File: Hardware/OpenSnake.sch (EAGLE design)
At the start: 36 parts, among them J1 microB, Q1 16MHZ, U1 ATMEGA328P_TQFP, U3 CH340G, U4 5V, Y2 12MHz

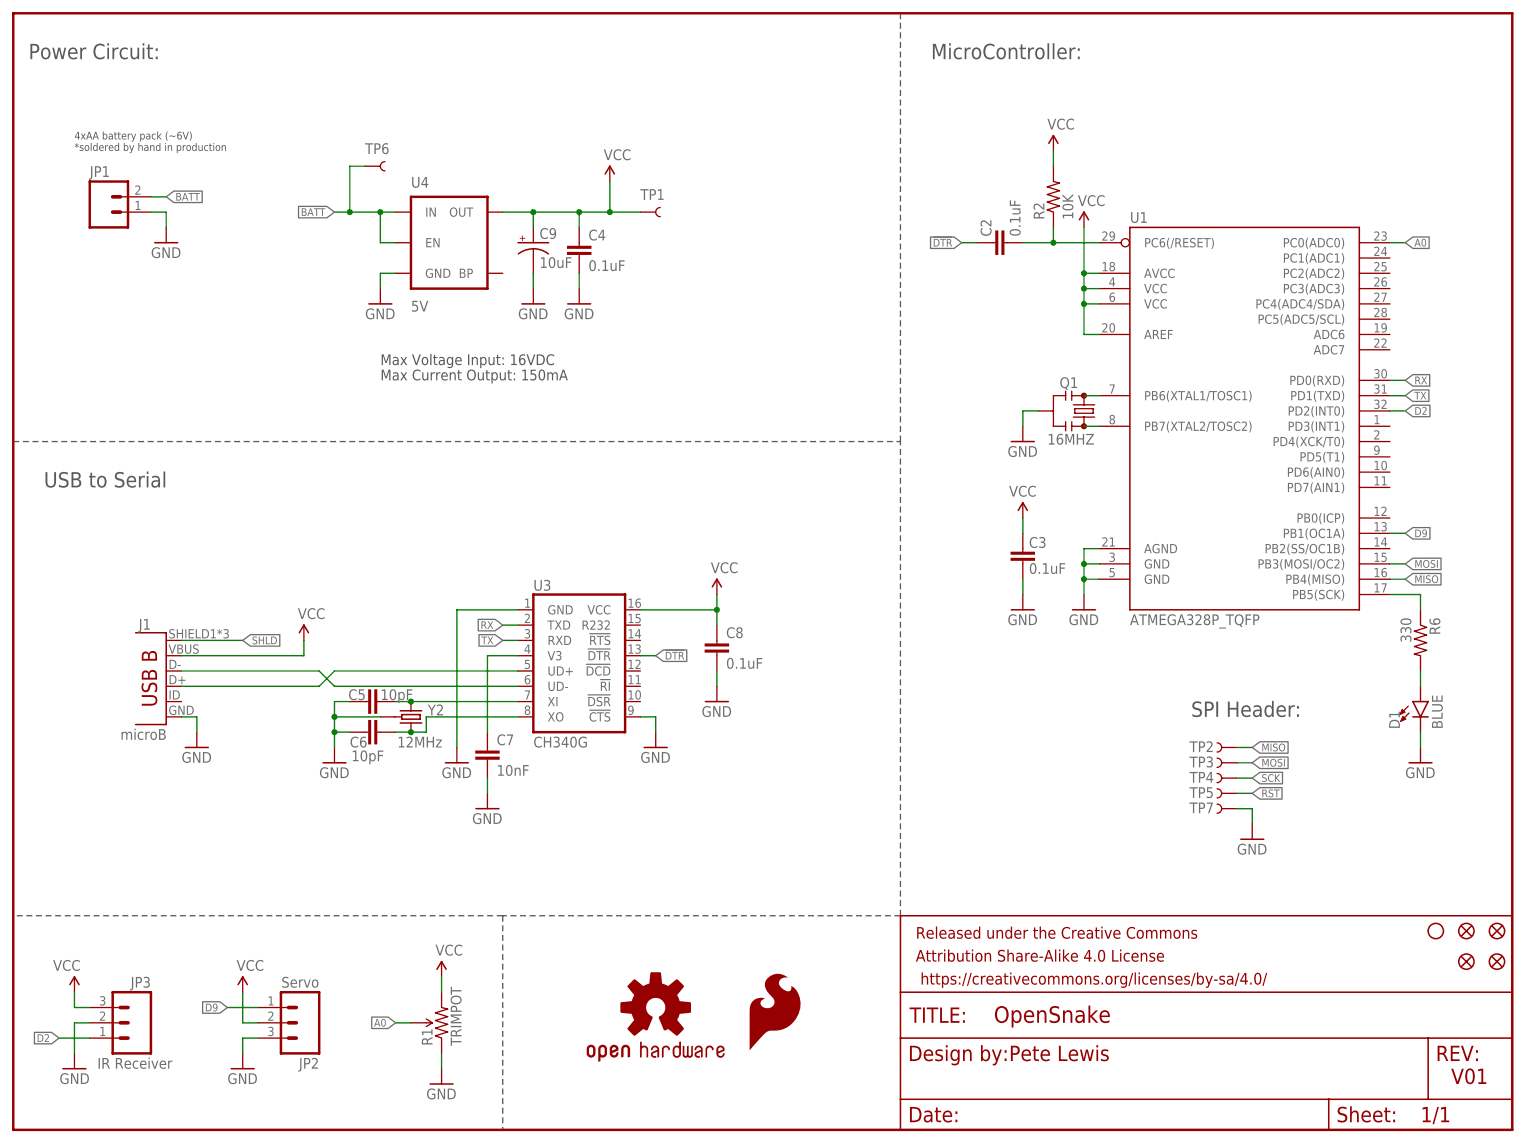
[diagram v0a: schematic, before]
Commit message: initial idea on pcb layout
the plan is to use some double sided tape and stick this to the side of the can. The 9V battery would also be stuck to the other side.
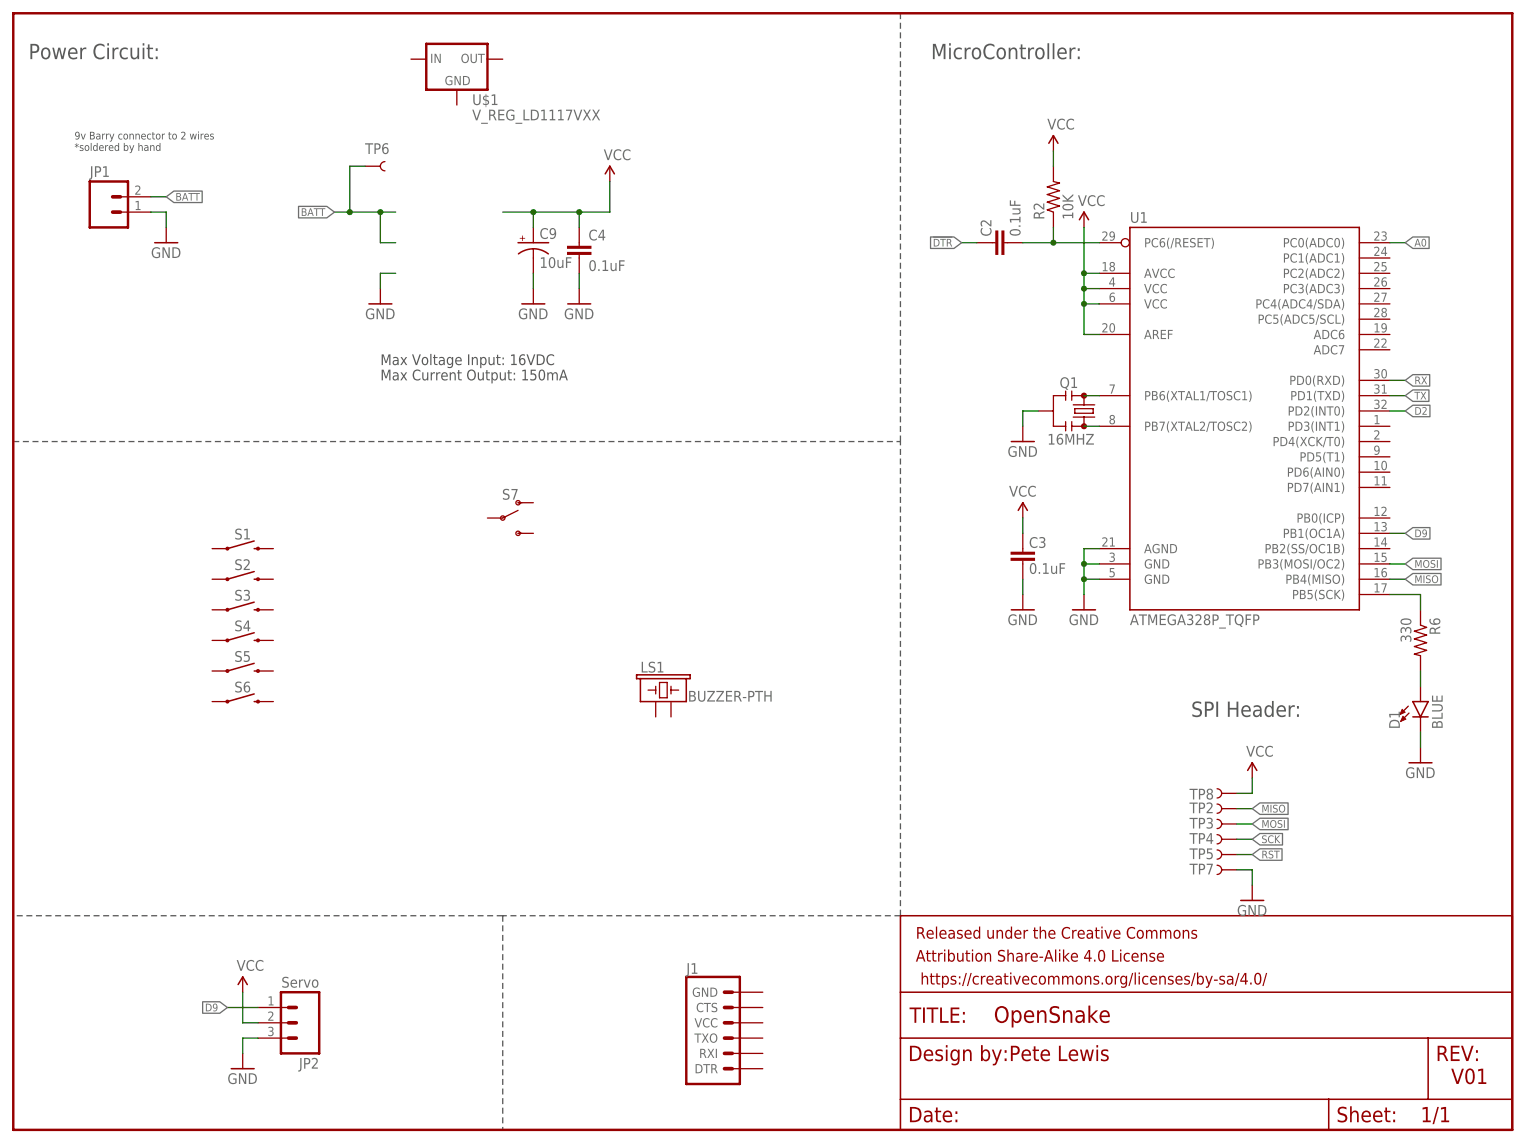
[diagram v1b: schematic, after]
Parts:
- removed C5, C6: 10pF, SparkFun-Capacitors:10PF-50V-5%(0603)
- removed C7: 10nF, SparkFun-Capacitors:10NF/10000PF-50V-10%(0603)
- removed C8: 0.1uF, SparkFun-Capacitors:0.1UF-25V(+80/-20%)(0603)
- removed FID1, FID2, FID3, FID4: FIDUCIALUFIDUCIAL, SparkFun-Aesthetics:FIDUCIALUFIDUCIAL
- removed H1: STAND-OFF, SparkFun-Hardware:STAND-OFF
- removed JP3: IR Receiver, Testing:M03LOCK
- removed LOGO1: SFE_LOGO_FLAME.1_INCH, SparkFun-Aesthetics:SFE_LOGO_FLAME.1_INCH
- removed LOGO2: OSHW-LOGOMINI, SparkFun-Aesthetics:OSHW-LOGOMINI
- removed R1: TRIMPOT, Jim-Resistors-to-Move:TRIMPOT-PTH-KNOB
- removed TP1: TEST-POINT3, SparkFun-Passives:TEST-POINT3
- removed U3: CH340G, SparkFun-DigitalIC:CH340GSMD
- removed U4: 5V, SparkFun-IC-Power:MIC52055V
- removed Y2: 12MHz, USB Basic:CRYSTAL-GROUNDED3.2X2.5
- added LS1: BUZZER-PTH, SparkFun-Electromechanical:BUZZER-PTH
- added S1, S2, S3, S4, S5, S6: MOMENTARY-SWITCH-SPST-PTH-6.0MM, SparkFun-Switches:MOMENTARY-SWITCH-SPST-PTH-6.0MM
- added S7: (no value), SparkFun-Switches:SWITCH-SPDT-PTH-11.6X4.0MM
- added TP8: TEST-POINT3, SparkFun-Passives:TEST-POINT3
- added U$1: V_REG_LD1117VXX, SparkFun-IC-Power:V_REG_LD1117VXX
- J1: value microB -> (none); device SparkFun-Connectors:USB-MICROB" -> SparkFun-Connectors:6_PIN_SERIAL_TARGETSILK
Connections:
- removed net N$3: C6.2, U3.XO, Y2.2
- removed net N$4: C5.2, U3.XI, Y2.1
- removed net N$5: J1.D+, U3.UD+
- removed net N$6: J1.D-, U3.UD-
- removed net SHLD: J1.SHIELD
- removed net V3: C7.1, U3.V3
- net !DTR: no longer U3.!DTR
- net A0: no longer R1.WIPER
- net BATT: no longer U4.EN, U4.IN
- net D2: no longer JP3.1
- net GND: no longer C5.1, C6.1, C7.2, C8.2, J1.GND, JP3.2, R1.CCW, U3.!CTS, U3.GND, U4.GND, Y2.GND
- net RX: no longer U3.TXD
- net TX: no longer U3.RXD
- net VCC: now also TP8.1; no longer C8.1, J1.VBUS, JP3.3, R1.CW, TP1.1, U3.VCC, U4.OUT
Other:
- note added: "9v Barry connector to 2 wires *soldered by hand"
- note removed: "4xAA battery pack (~6V) *soldered by hand in production"
- note removed: "USB to Serial"
- moved on the sheet: TP2, TP3, TP4, TP5, TP7

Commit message: v01 hardware ordered - Added mario logo to bottom silk -  and code started
-mario logo on bottom silk
-v01 hardware prototypes ordered
-Started working on the code using a simon says kit.
-got yes, no sound functions working
-got default tracks working and playing
-still needs servo control implemented, but currently mapped out in snake() function
-still needs button control, record feature and factory reset feature
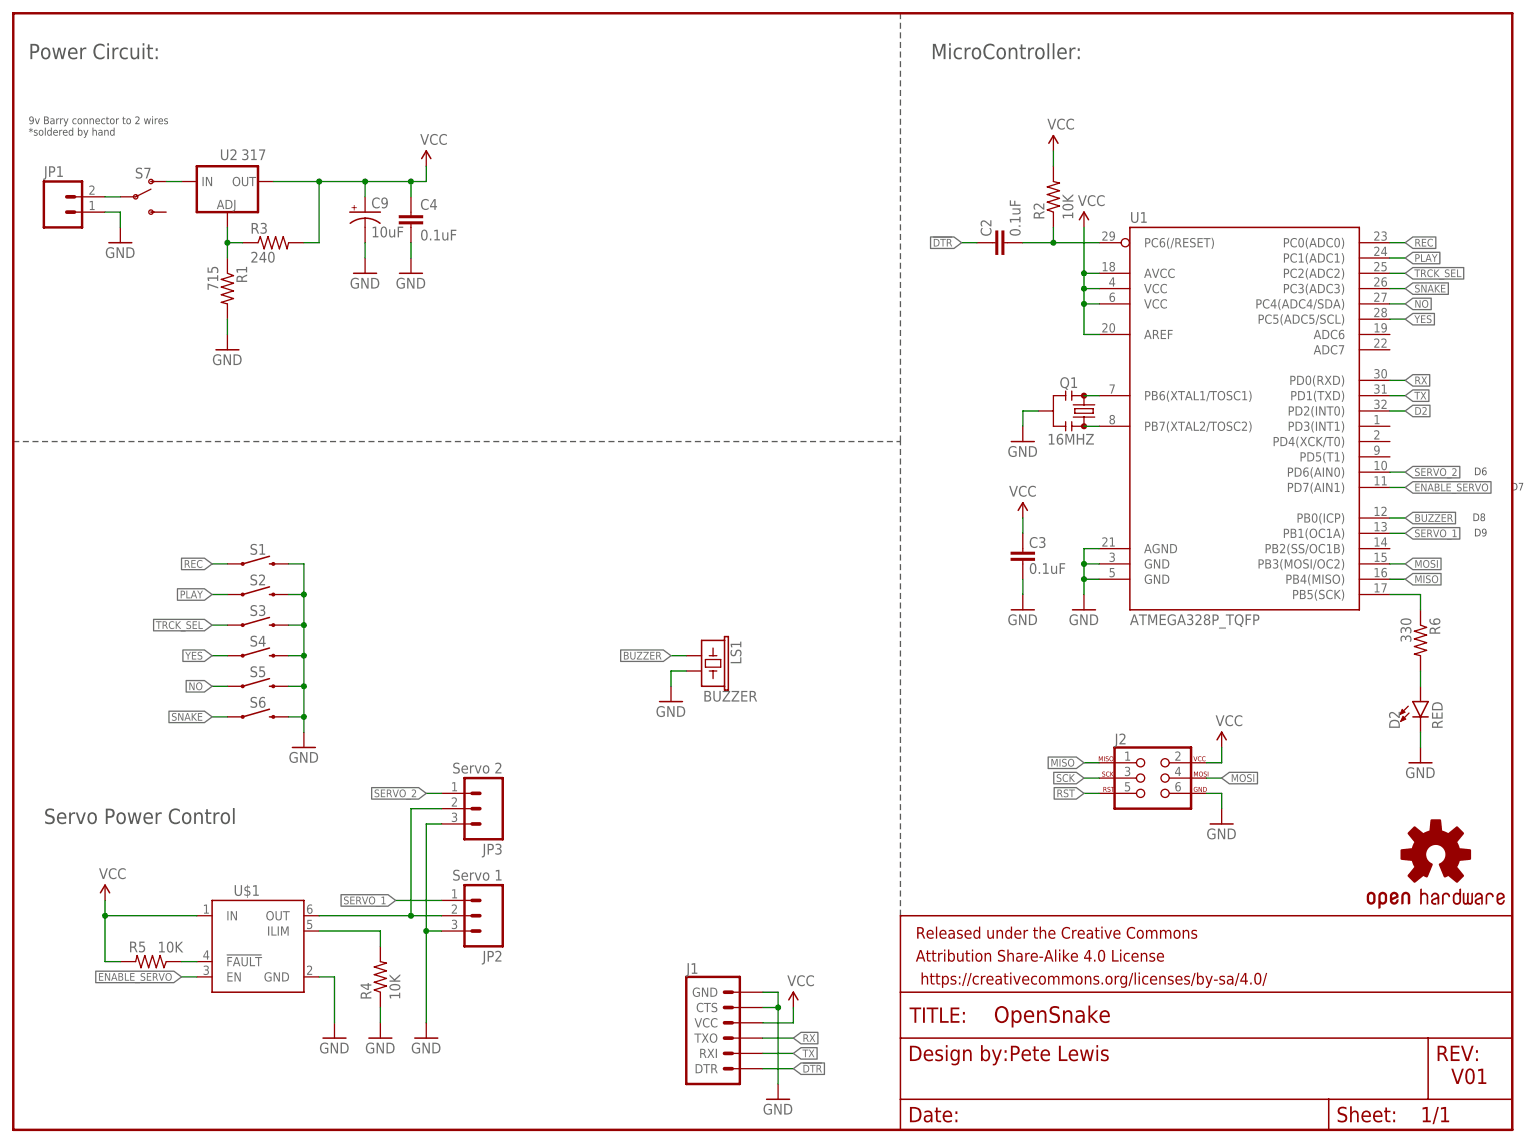
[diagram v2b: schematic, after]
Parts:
- removed D1: BLUE, SparkFun-LED:LED-BLUE1206
- removed TP2, TP3, TP4, TP5, TP6, TP7, TP8: TEST-POINT3, SparkFun-Passives:TEST-POINT3
- added D2: RED, SparkFun-LED:LED10MM
- added J2: AVR_SPI_PROG_3X2PTH, SparkFun-Connectors:AVR_SPI_PROG_3X2PTH
- added JP3: Servo 2, Testing:M03LOCK
- added LOGO1: OSHW-LOGOL, SparkFun-Aesthetics:OSHW-LOGOL
- added R1: 715, SparkFun-Resistors:330OHM1/10W1%(0603)
- added R3: 240, SparkFun-Resistors:330OHM1/10W1%(0603)
- added R4, R5: 10K, SparkFun-Resistors:10KOHM-1/10W-1%(0603)0603
- added U2: 317, SparkFun-IC-Power:V_REG_317SINK
- JP2: value Servo -> Servo 1
- LS1: value BUZZER-PTH -> BUZZER
- S1, S2, S3, S4, S5, S6: value MOMENTARY-SWITCH-SPST-PTH-6.0MM -> MOMENTARY-SWITCH-SPST-SMD-5.2MM-TALL; device SparkFun-Switches:MOMENTARY-SWITCH-SPST-PTH-6.0MM -> SparkFun-Switches:MOMENTARY-SWITCH-SPST-SMD-5.2MM-TALL
- U$1: value V_REG_LD1117VXX -> AP2553; device SparkFun-IC-Power:V_REG_LD1117VXX -> snake:AP2553
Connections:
- net D9 renamed SERVO_1
- removed net A0: U1.PC0(ADC0)
- removed net BATT: JP1.2, TP6.1
- new net BUZZER: LS1.1, U1.PB0(ICP)
- new net ENABLE_SERVO: U$1.EN, U1.PD7(AIN1)
- new net N$3: R1.1, R3.1, U2.ADJ
- new net N$4: JP1.2, S7.P
- new net N$5: S7.O, U2.IN
- new net N$6: JP2.2, JP3.2, U$1.OUT
- new net N$8: R4.2, U$1.ILIM
- new net N$9: R5.1, U$1.!FAULT
- new net NO: S5.1, U1.PC4(ADC4/SDA)
- new net PLAY: S2.1, U1.PC1(ADC1)
- new net REC: S1.1, U1.PC0(ADC0)
- new net SERVO_2: JP3.1, U1.PD6(AIN0)
- new net SNAKE: S6.1, U1.PC3(ADC3)
- new net TRCK_SEL: S3.1, U1.PC2(ADC2)
- new net YES: S4.1, U1.PC5(ADC5/SCL)
- net !DTR: now also J1.DTR
- net GND: now also D2.C, J1.CTS, J1.GND, J2.6, JP3.3, LS1.2, R1.2, R4.1, S1.2, S2.2, S3.2, S4.2, S5.2, S6.2, U$1.GND; no longer D1.C, TP7.1
- net MISO: now also J2.1; no longer TP2.1
- net MOSI: now also J2.4; no longer TP3.1
- net N$7: now also D2.A; no longer D1.A
- net RST: now also J2.5; no longer TP5.1
- net RX: now also J1.TXO
- net SCK: now also J2.3; no longer TP4.1
- net TX: now also J1.RXI
- net VCC: now also J1.VCC, J2.2, R3.2, R5.2, U$1.IN, U2.OUT; no longer JP2.2, TP8.1
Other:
- note added: "D6"
- note added: "D7"
- note added: "D8"
- note added: "D9"
- note added: "Servo Power Control"
- note removed: "Max Current Output: 150mA"
- note removed: "Max Voltage Input: 16VDC"
- note removed: "SPI Header:"
- moved on the sheet: C4, C9, JP1, JP2, LS1, S1, S2, S3, S4, S5, S6, S7

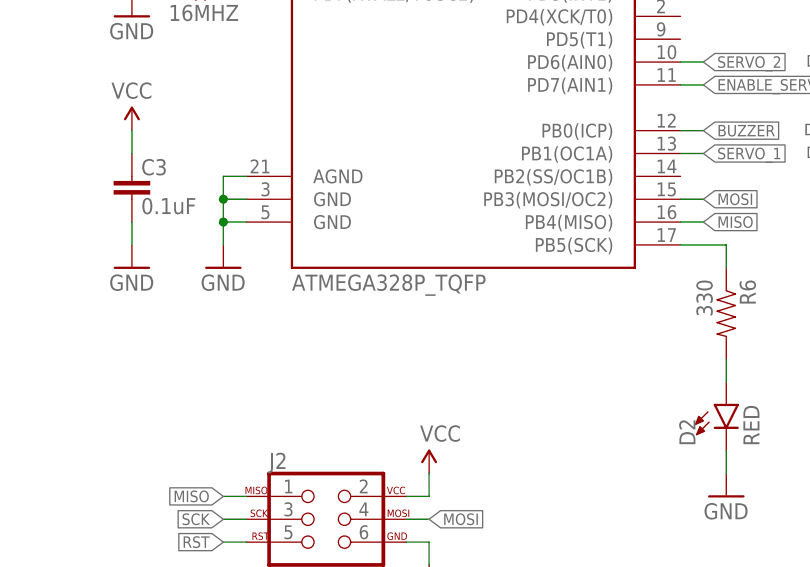
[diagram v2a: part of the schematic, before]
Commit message: Adjusted tValues for better assembly sheet, created assembly sheet PDF
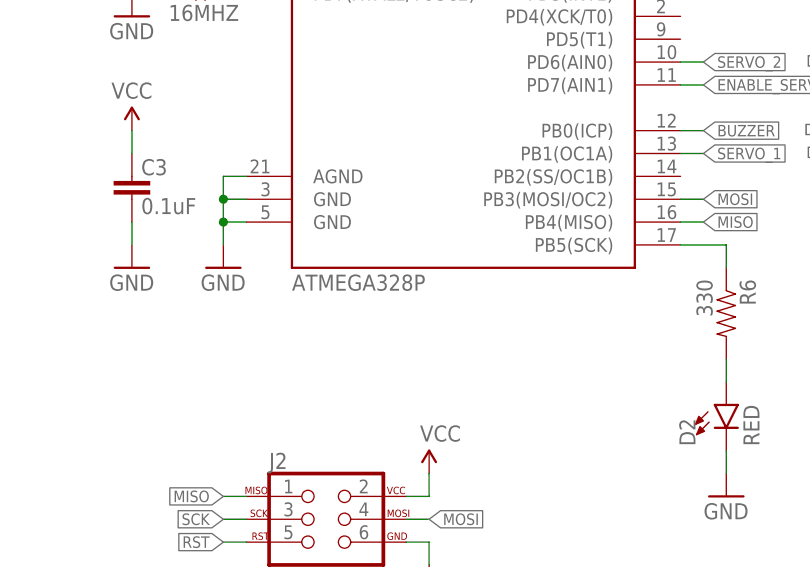
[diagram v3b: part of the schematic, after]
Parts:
- U1: value ATMEGA328P_TQFP -> ATMEGA328P
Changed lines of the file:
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@@
 <part name="GND5" library="SparkFun" deviceset="GND" device=""/>
 <part name="C2" library="SparkFun-Capacitors" deviceset="0.1UF-25V(+80/-20%)(0603)" device="" value="0.1uF"/>
-<part name="U1" library="SparkFun-DigitalIC" deviceset="ATMEGA328P_TQFP" device="" value="ATMEGA328P_TQFP"/>
+<part name="U1" library="SparkFun-DigitalIC" deviceset="ATMEGA328P_TQFP" device="" value="ATMEGA328P"/>
 <part name="JP1" library="Testing" deviceset="M02" device="PTH"/>
 <part name="GND6" library="SparkFun" deviceset="GND" device=""/>
